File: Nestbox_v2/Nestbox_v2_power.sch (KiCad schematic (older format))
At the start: 10 parts

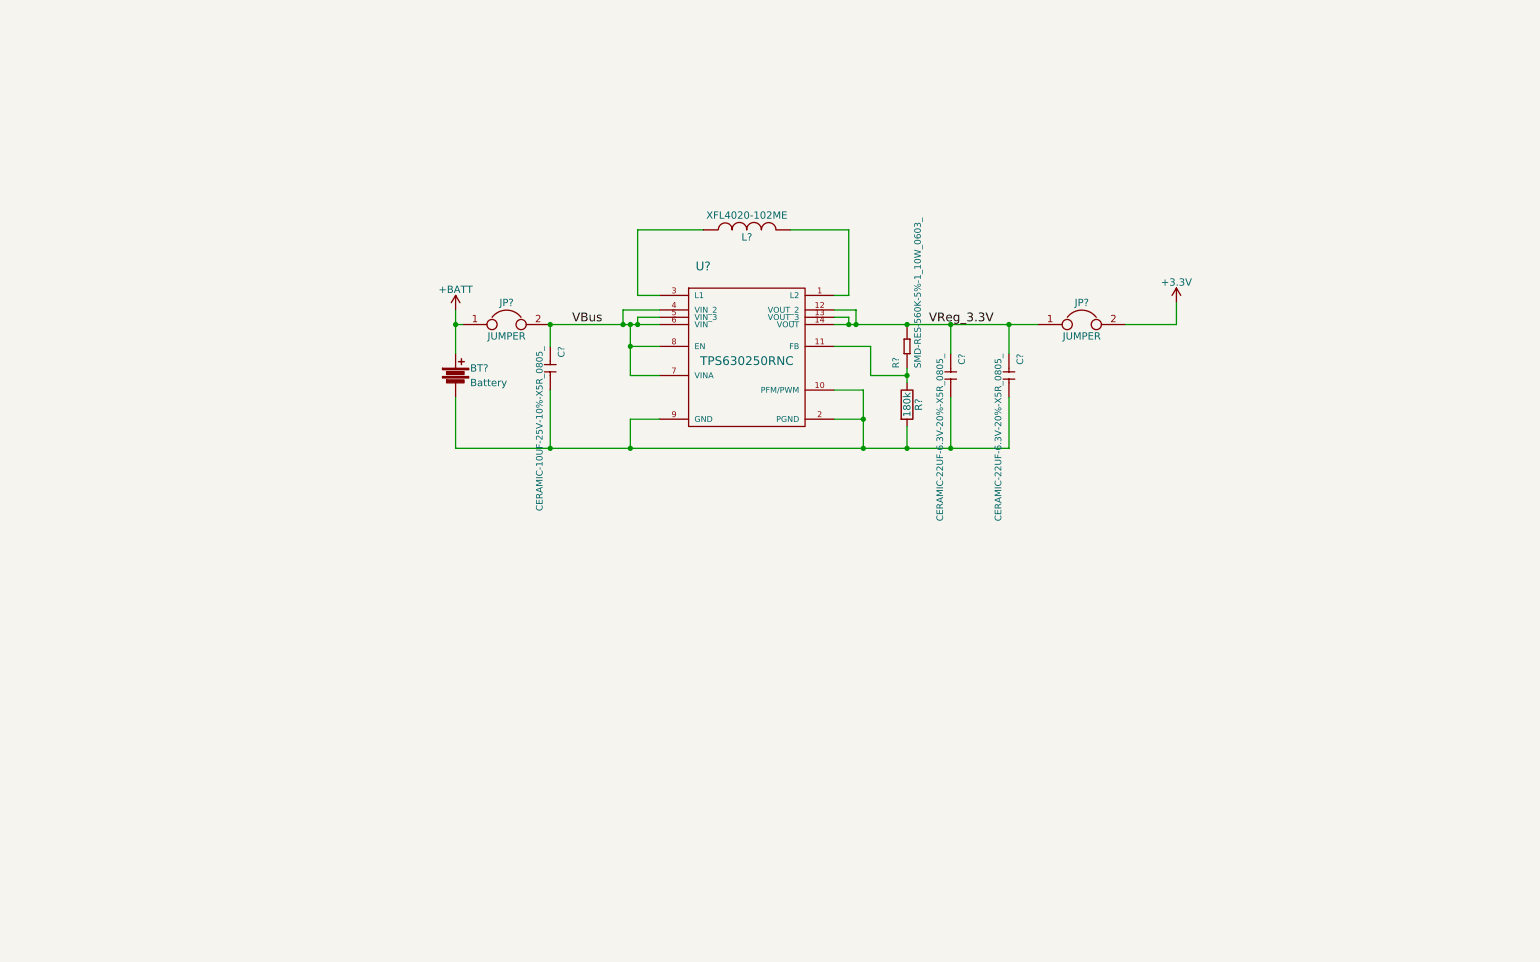
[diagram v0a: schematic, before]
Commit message: Adds Solar power harvester circuit
The bq25504 is used for solar power harvesting and battery management.
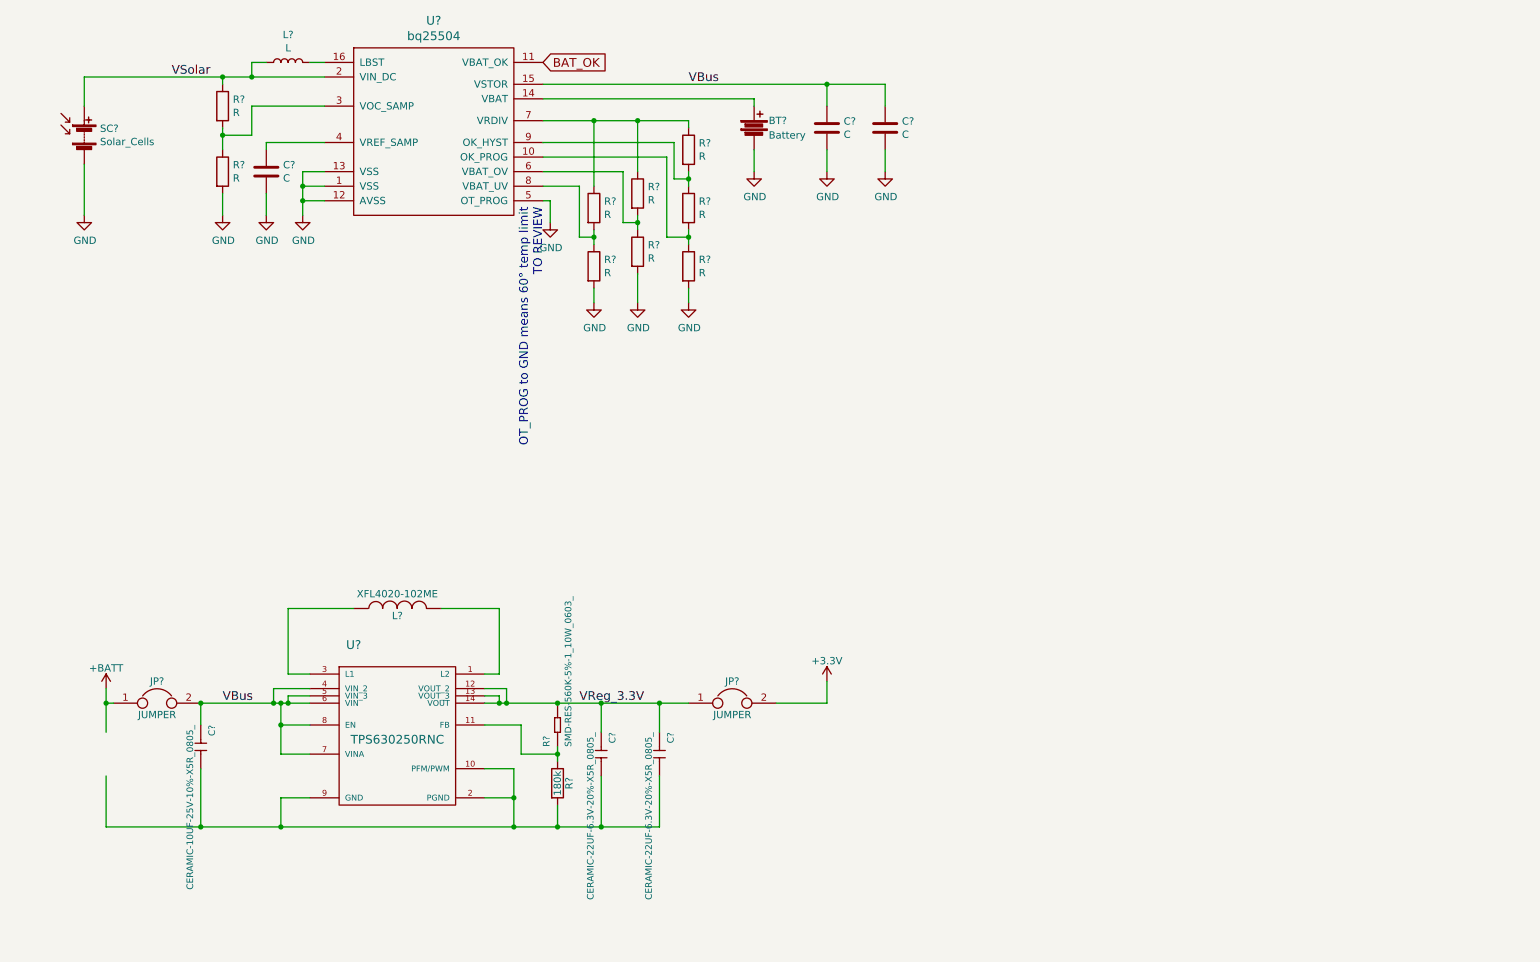
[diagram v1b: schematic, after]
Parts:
- added C? (x3): C, symbol C
- added L?: L, symbol L
- added R? (x9): R, symbol R
- added SC?: Solar_Cells, symbol Solar_Cells
- added U?: bq25504, symbol bq25504
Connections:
- net +BATT: no longer BT?.1
- net VBus: now also C?.1, C?.1, U?.15 (VSTOR)
- net at C?.2, C?.2, C?.2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: no longer BT?.2
- new net: BT?.1, U?.14 (VBAT)
- new net: R?.1, R?.2, U?.3 (VOC_SAMP)
- new net: C?.1, U?.4 (VREF_SAMP)
- new net: L?.2, U?.16 (LBST)
- new net: R?.1, R?.1, R?.1, U?.7 (VRDIV)
- new net: R?.1, R?.2, U?.9 (OK_HYST)
- new net: R?.1, R?.2, U?.10 (OK_PROG)
- new net: R?.1, R?.2, U?.6 (VBAT_OV)
- new net: R?.1, R?.2, U?.8 (VBAT_UV)
- new net BAT_OK: U?.11 (VBAT_OK)
- new net GND: BT?.2, C?.2, C?.2, C?.2, R?.2, R?.2, R?.2, R?.2, SC?.2 (-), U?.1 (VSS), U?.12 (AVSS), U?.13 (VSS), U?.5 (OT_PROG)
- new net VSolar: L?.1, R?.1, SC?.1 (+), U?.2 (VIN_DC)
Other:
- note added: "OT_PROG to GND means 60° temp limit\nTO REVIEW"
- moved on the sheet: BT?, C?, JP?, L?, R?, U?

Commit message: Adds 3.3 and 5V regulators to power schematic
TPS63050 for 5V
TPS63051 for 3.3V

Need to finish calculating the R and C values
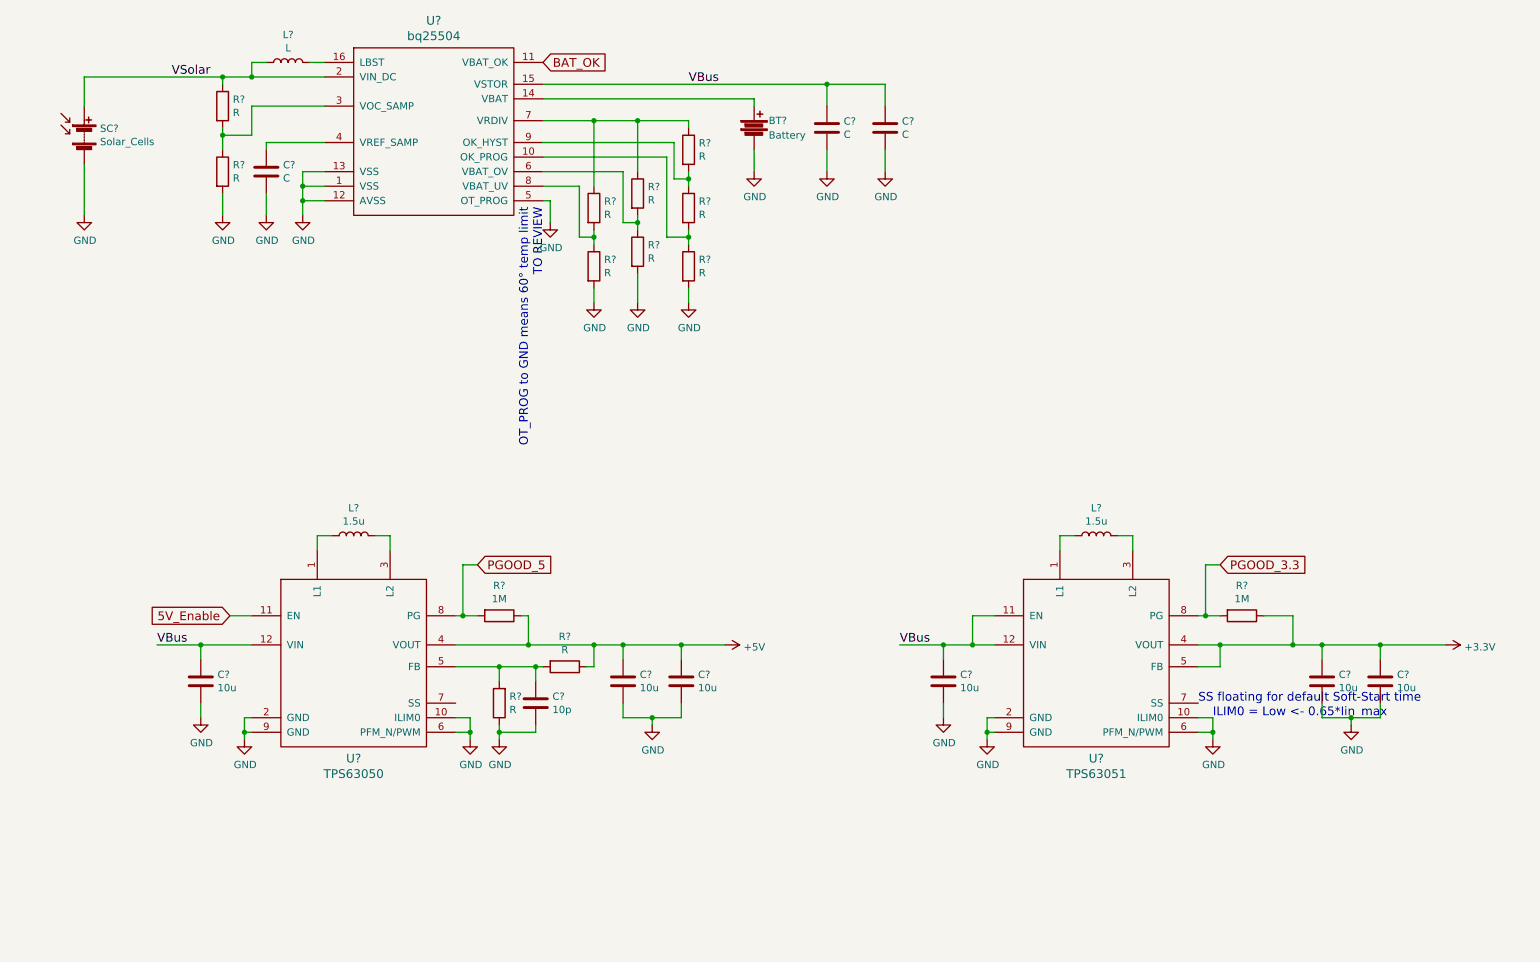
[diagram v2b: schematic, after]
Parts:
- removed C?: CERAMIC-10UF-25V-10%-X5R_0805_, SeeedOPL-Capacitor-2016:C0805, symbol CERAMIC-10UF-25V-10%-X5R_0805_
- removed C? (x2): CERAMIC-22UF-6.3V-20%-X5R_0805_, SeeedOPL-Capacitor-2016:C0805, symbol CERAMIC-22UF-6.3V-20%-X5R_0805_
- removed JP? (x2): JUMPER, Socket_Strips:Socket_Strip_Straight_1x02, symbol Jumper
- removed L?: XFL4020-102ME, Octanis3:XFL4020, symbol INDUCTOR
- removed R?: SMD-RES-560K-5%-1_10W_0603_, SeeedOPL-Resistor-2016:R0603, symbol SMD-RES-560K-5%-1_10W_0603_
- removed R?: 180k, Resistors_SMD:R_0603, symbol R
- removed U?: TPS630250RNC, Octanis3:RNC0014A, symbol TPS630250RNC
- added C? (x6): 10u, symbol C
- added C?: 10p, symbol C
- added L? (x2): 1.5u, symbol L
- added R? (x2): 1M, symbol R
- added R? (x2): R, symbol R
- added U?: TPS63051, symbol TPS63051
- added U?: TPS63050, symbol TPS63050
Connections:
- net +3V3: now also C?.1, C?.1, R?.1, U?.4 (VOUT), U?.5 (FB)
- net GND: now also C?.2, C?.2, C?.2, C?.2, C?.2, C?.2, C?.2, R?.1, U?.10 (ILIM0), U?.10 (ILIM0), U?.2 (GND), U?.2 (GND), U?.6 (PFM_N/PWM), U?.6 (PFM_N/PWM), U?.9 (GND), U?.9 (GND)
- net VBus: now also C?.1, C?.1, U?.11 (EN), U?.12 (VIN), U?.12 (VIN)
- new net: L?.1, U?.1 (L1) (x2)
- new net: L?.2, U?.3 (L2) (x2)
- new net: C?.1, R?.2, R?.2, U?.5 (FB)
- new net +5V: C?.1, C?.1, R?.1, R?.1, U?.4 (VOUT)
- new net 5V_Enable: U?.11 (EN)
- new net PGOOD_3.3: R?.2, U?.8 (PG)
- new net PGOOD_5: R?.2, U?.8 (PG)
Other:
- note added: "ILIM0 = Low <- 0.65*Iin_max"
- note added: "SS floating for default Soft-Start time"

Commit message: Adds Power domain jumpers and HK resistive dividers
- Jumpers have been added around all power supply chips, in order to
isolate certain power domains.
- Resistive dividers are added to connect ADC for HK
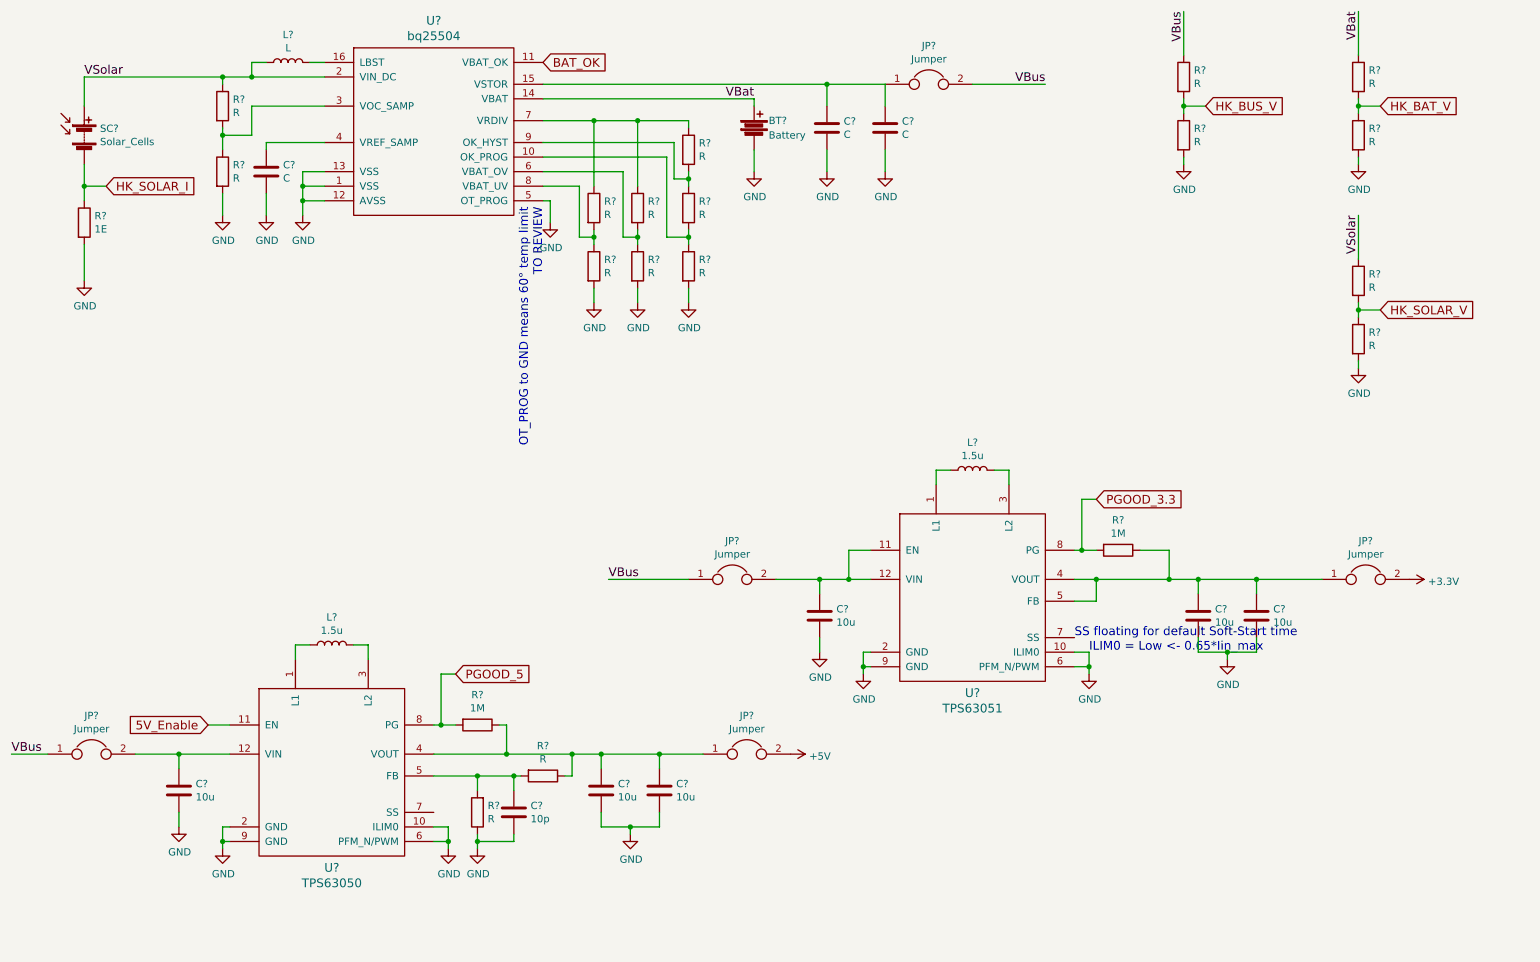
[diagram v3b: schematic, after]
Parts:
- added JP? (x5): Jumper, symbol Jumper
- added R?: 1E, symbol R
- added R? (x6): R, symbol R
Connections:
- net +3V3: now also JP?.2; no longer C?.1, C?.1, R?.1, U?.4 (VOUT), U?.5 (FB)
- net +5V: now also JP?.2; no longer C?.1, C?.1, R?.1, R?.1, U?.4 (VOUT)
- net GND: now also R?.2, R?.2, R?.2, R?.2; no longer SC?.2 (-)
- net VBus: now also JP?.1, JP?.1, JP?.2, R?.1; no longer C?.1, C?.1, C?.1, C?.1, U?.11 (EN), U?.12 (VIN), U?.12 (VIN), U?.15 (VSTOR)
- net VSolar: now also R?.1
- net VBat: now reaches BT?.1, U?.14 (VBAT)
- net VBat: now also R?.1
- new net: C?.1, C?.1, JP?.1, U?.15 (VSTOR)
- new net: C?.1, JP?.2, U?.12 (VIN)
- new net: C?.1, JP?.2, U?.11 (EN), U?.12 (VIN)
- new net: C?.1, C?.1, JP?.1, R?.1, R?.1, U?.4 (VOUT)
- new net: C?.1, C?.1, JP?.1, R?.1, U?.4 (VOUT), U?.5 (FB)
- new net HK_BAT_V: R?.1, R?.2
- new net HK_BUS_V: R?.1, R?.2
- new net HK_SOLAR_I: R?.1, SC?.2 (-)
- new net HK_SOLAR_V: R?.1, R?.2
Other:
- moved on the sheet: C?, L?, R?, U?

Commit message: Annotated power schematic
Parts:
- gave numbers to parts that had none: 43

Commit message: Annotated entire schematic
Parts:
- renumbered BT1 to BT201, C1 to C201, C2 to C202, C3 to C203, C4 to C204, C5 to C205, C6 to C206, C7 to C207, C8 to C208, C9 to C209, C10 to C210, JP1 to JP201, JP2 to JP202, JP3 to JP203, JP4 to JP204, JP5 to JP205, L1 to L201, L2 to L202, L3 to L203, R1 to R201, R2 to R202, R3 to R203, R4 to R204, R5 to R205, R6 to R206, R7 to R207, R8 to R208, R9 to R209, R10 to R210, R11 to R211, R12 to R212, R13 to R213, R14 to R214, R15 to R215, R16 to R216, R17 to R217, R18 to R218, R19 to R219, R20 to R220, SC1 to SC201, U1 to U201, U2 to U202, U3 to U203
